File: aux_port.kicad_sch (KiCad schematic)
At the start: 33 parts, among them IC1 ECP5-BGA256, J5 MEZZANINE, U11 USB3343-CP, U12 FUSB302B, U14 DPO2036

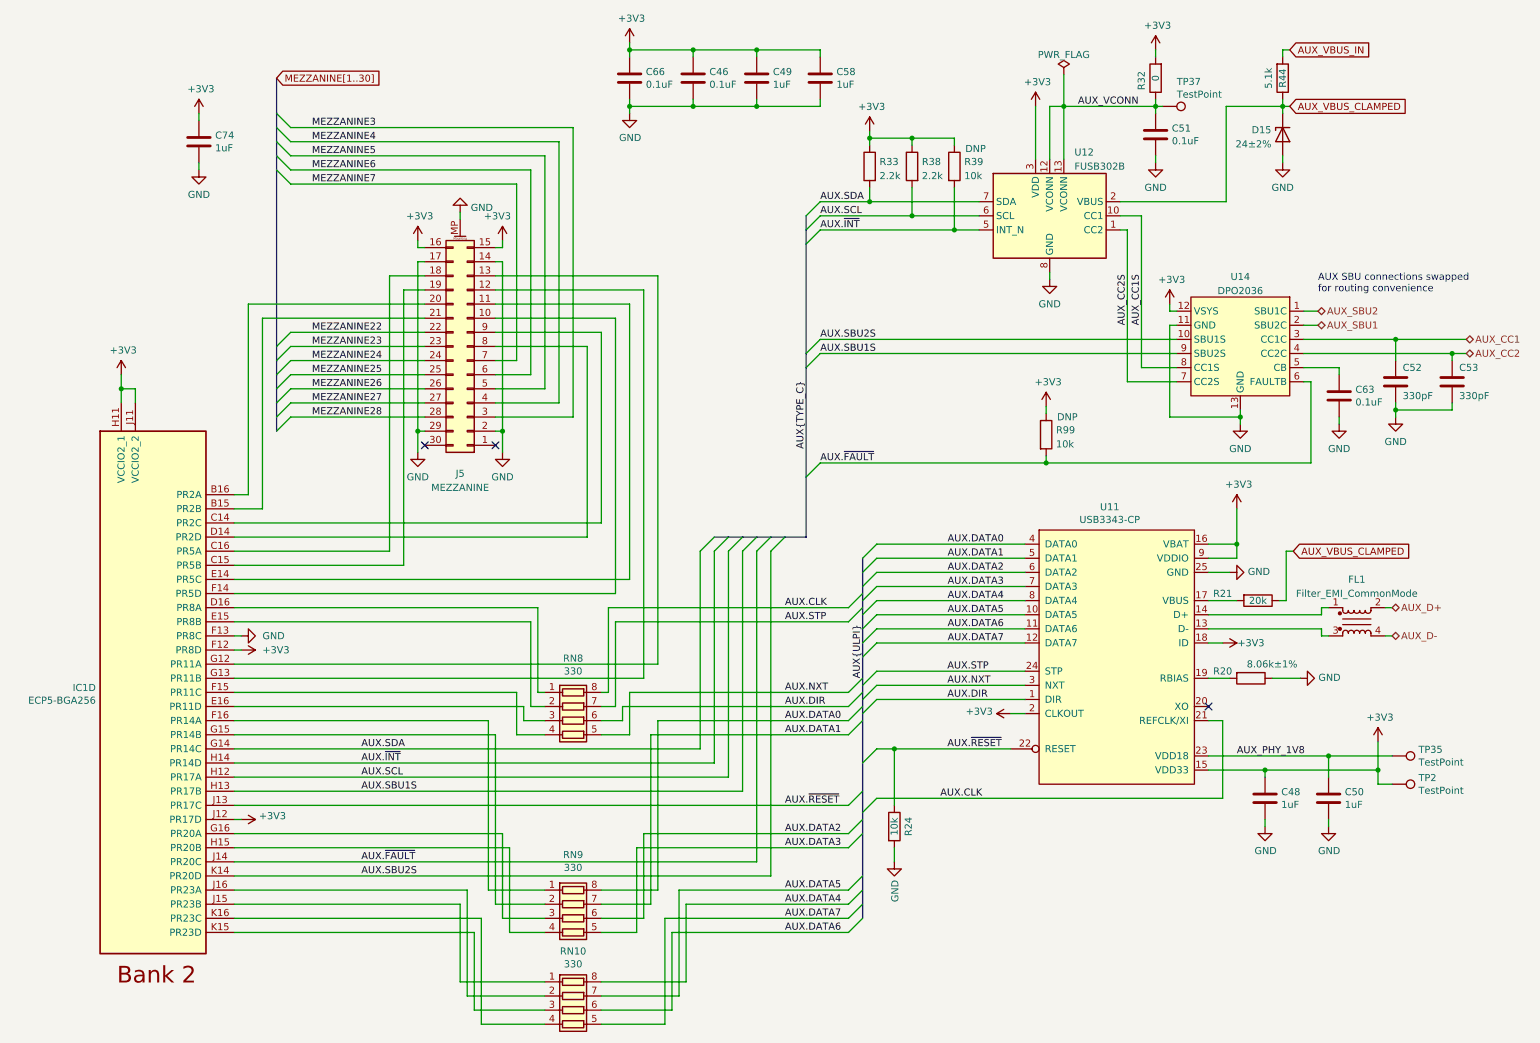
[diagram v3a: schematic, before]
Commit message: Rearrange schematic for readability
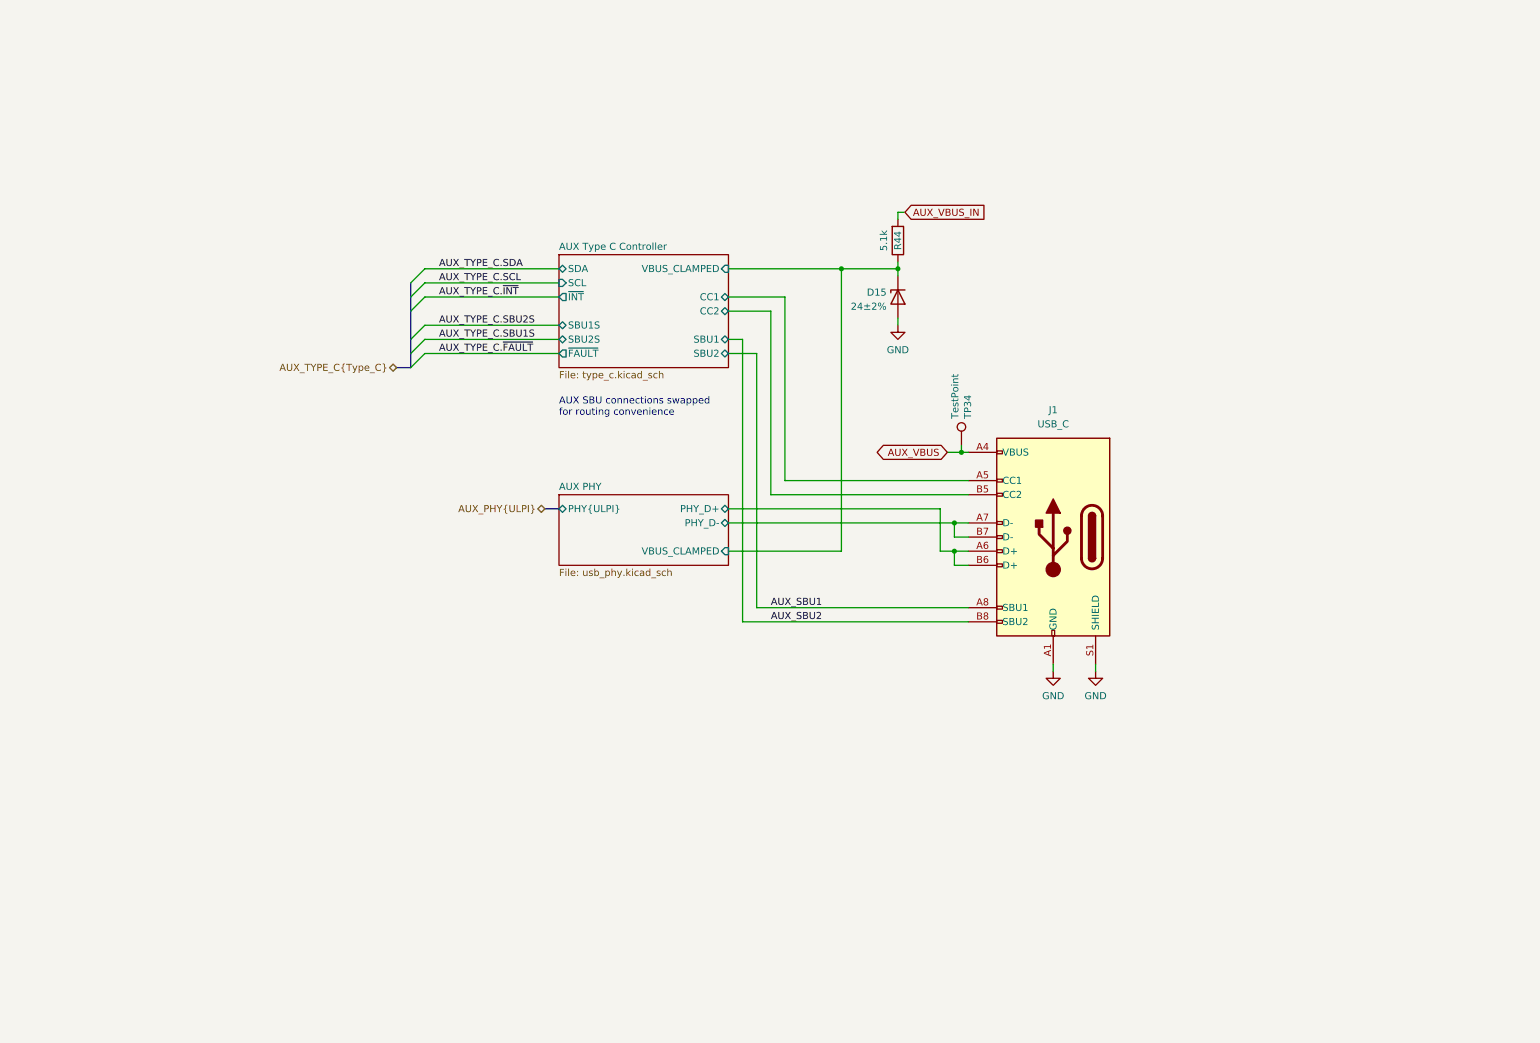
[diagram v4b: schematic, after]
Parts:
- removed C46, C51, C63, C66: 0.1uF, Capacitor_SMD:C_0402_1005Metric, symbol Device:C
- removed C48, C49, C50, C58, C74: 1uF, Capacitor_SMD:C_0402_1005Metric, symbol Device:C
- removed C52, C53: 330pF, Capacitor_SMD:C_0402_1005Metric, symbol Device:C
- removed FL1: Filter_EMI_CommonMode, cynthion:L_CommonModeChoke_Murata_DLM0NS, symbol Device:Filter_EMI_CommonMode
- removed IC1: ECP5-BGA256, cynthion:lattice_cabga256, symbol fpgas_and_processors:ECP5-BGA256
- removed J5: MEZZANINE, cynthion:Amphenol_10132798-03, symbol Connector_Generic_MountingPin:Conn_02x15_Counter_Clockwise_MountingPin
- removed R20: 8.06k±1%, Resistor_SMD:R_0402_1005Metric, symbol Device:R
- removed R21: 20k, Resistor_SMD:R_0402_1005Metric, symbol Device:R
- removed R24, R39, R99: 10k, Resistor_SMD:R_0402_1005Metric, symbol Device:R
- removed R32: 0, Resistor_SMD:R_0402_1005Metric, symbol Device:R
- removed R33, R38: 2.2k, Resistor_SMD:R_0402_1005Metric, symbol Device:R
- removed RN10, RN8, RN9: 330, Resistor_SMD:R_Array_Convex_4x0402, symbol Device:R_Pack04
- removed TP2, TP35, TP37: TestPoint, TestPoint:TestPoint_Pad_D1.0mm, symbol Connector:TestPoint
- removed U11: USB3343-CP, Package_DFN_QFN:VQFN-24-1EP_4x4mm_P0.5mm_EP2.45x2.45mm, symbol usb:USB3343
- removed U12: FUSB302B, Package_DFN_QFN:WQFN-14-1EP_2.5x2.5mm_P0.5mm_EP1.45x1.45mm, symbol Interface_USB:FUSB302BMPX
- removed U14: DPO2036, cynthion:Diodes_UQFN2020-12_Type-B, symbol usb:DPO2036
- added J1: USB_C, cynthion:USB_C_Receptacle_HRO_TYPE-C-31-M-12, symbol Connector:USB_C_Receptacle_USB2.0
- added TP34: TestPoint, TestPoint:TestPoint_Pad_D1.0mm, symbol Connector:TestPoint
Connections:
- net AUX_SBU1: now also J1.A8 (SBU1)
- net AUX_SBU2: now also J1.B8 (SBU2)
- net GND: now also J1.A1 (GND), J1.A12 (GND), J1.B1 (GND), J1.B12 (GND), J1.S1 (SHIELD)
- net AUX_VBUS_CLAMPED renamed AUX PHY/VBUS_CLAMPED
- new net AUX PHY/PHY_D+: J1.A6 (D+), J1.B6 (D+)
- new net AUX PHY/PHY_D-: J1.A7 (D-), J1.B7 (D-)
- new net AUX Type C Controller/CC1: J1.A5 (CC1)
- new net AUX Type C Controller/CC2: J1.B5 (CC2)
- new net AUX_VBUS: J1.A4 (VBUS), J1.A9 (VBUS), J1.B4 (VBUS), J1.B9 (VBUS), TP34.1
- no-connect marks 3 -> 0
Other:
- added sheet AUX PHY (usb_phy.kicad_sch)
- added sheet AUX Type C Controller (type_c.kicad_sch)
- moved on the sheet: D15, R44

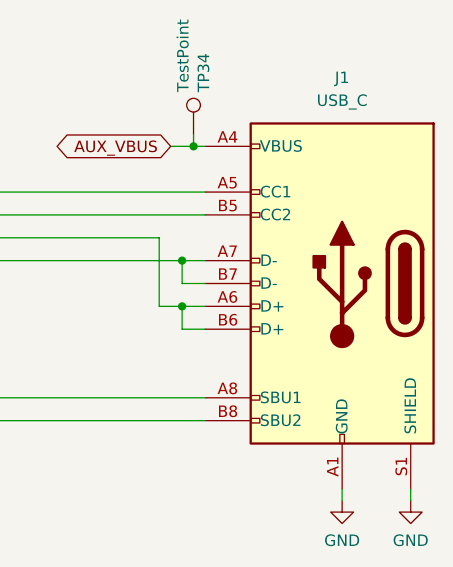
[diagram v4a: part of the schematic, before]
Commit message: Upgrade to KiCad 7
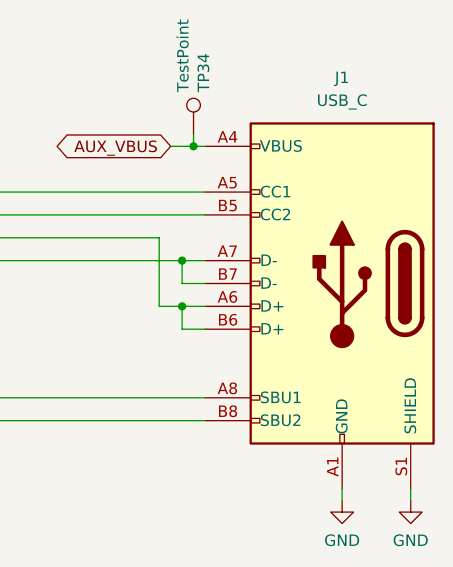
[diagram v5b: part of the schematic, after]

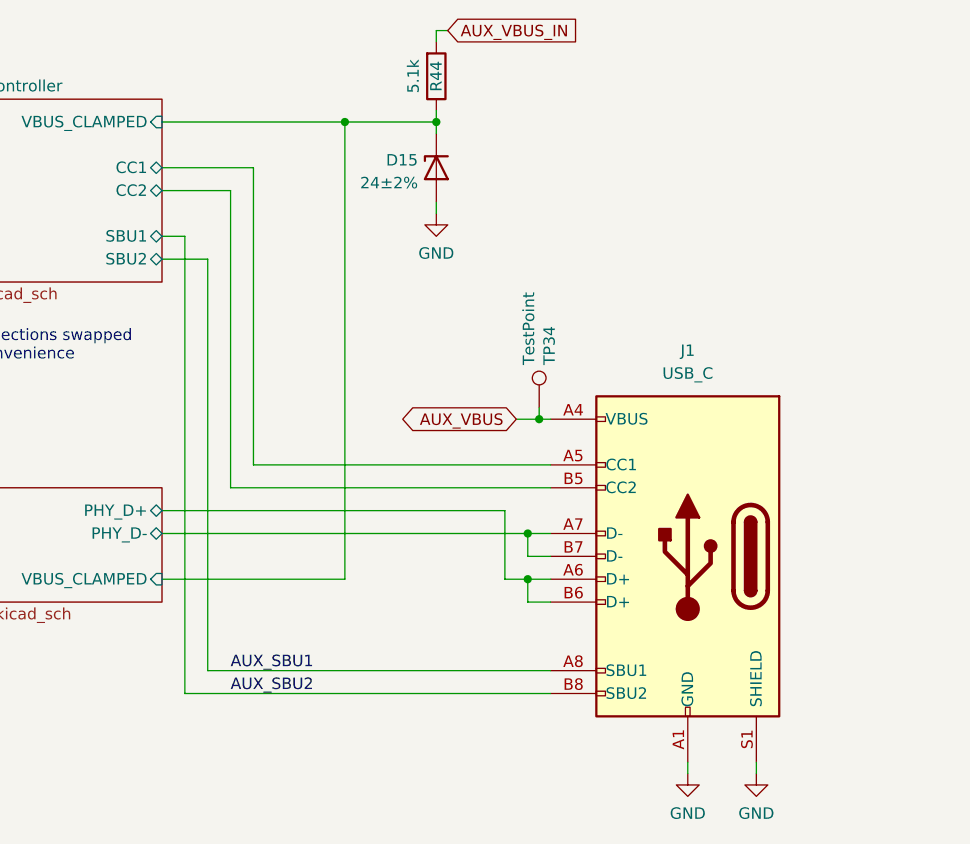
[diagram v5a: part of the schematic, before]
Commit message: Use four-terminal current sense resistor symbol
Previously we had used a special four-terminal symbol and footprint to
ensure that current sense signals did not connect to power supply zones
in multiple places. We rejected this in favor of a two-terminal
schematic symbol and standard resistor footprint to ensure reliable
assembly.

This new solution uses a four-terminal schematic symbol with a
two-terminal footprint which is actually four terminals in two
overlapping pairs using the "net tie" footprint feature.

Fixes #13
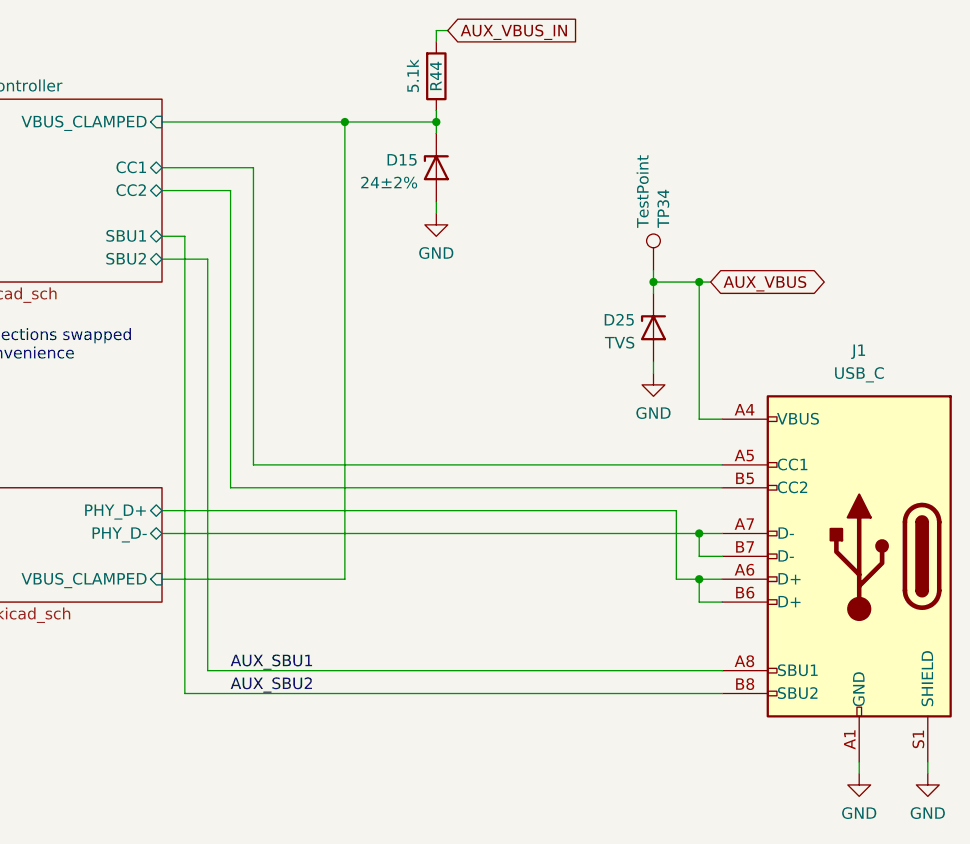
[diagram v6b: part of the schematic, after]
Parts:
- added D25: TVS, cynthion:DFN1006-2, symbol Device:D_Zener
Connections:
- net AUX_VBUS: now also D25.1 (K)
- net GND: now also D25.2 (A)
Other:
- moved on the sheet: J1, TP34
